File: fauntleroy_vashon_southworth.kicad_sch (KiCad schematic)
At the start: 48 parts

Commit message: pier 50 routing checkpoint
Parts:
- added LED533, LED595: WS2812B-2020, EasyEDA:LED-SMD_4P-L2.0-W2.0-TL_WS2812B-2020, symbol EasyEDA:WS2812B-2020
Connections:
- net +VLED: now also LED533.4 (VDD), LED595.4 (VDD)
- net GND: now also LED533.2 (GND), LED595.2 (GND)
- net at LED581.1 (DO): now also LED595.3 (DI)
- net at LED531.1 (DO): now also LED533.3 (DI)

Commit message: single ferry track checkpoint
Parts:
- removed LED533, LED559, LED560, LED561, LED562, LED563, LED564, LED565, LED566, LED567, LED568, LED569, LED570, LED571, LED572, LED573, LED574, LED576, LED577, LED578, LED579, LED580, LED581, LED595: WS2812B-2020, EasyEDA:LED-SMD_4P-L2.0-W2.0-TL_WS2812B-2020, symbol EasyEDA:WS2812B-2020

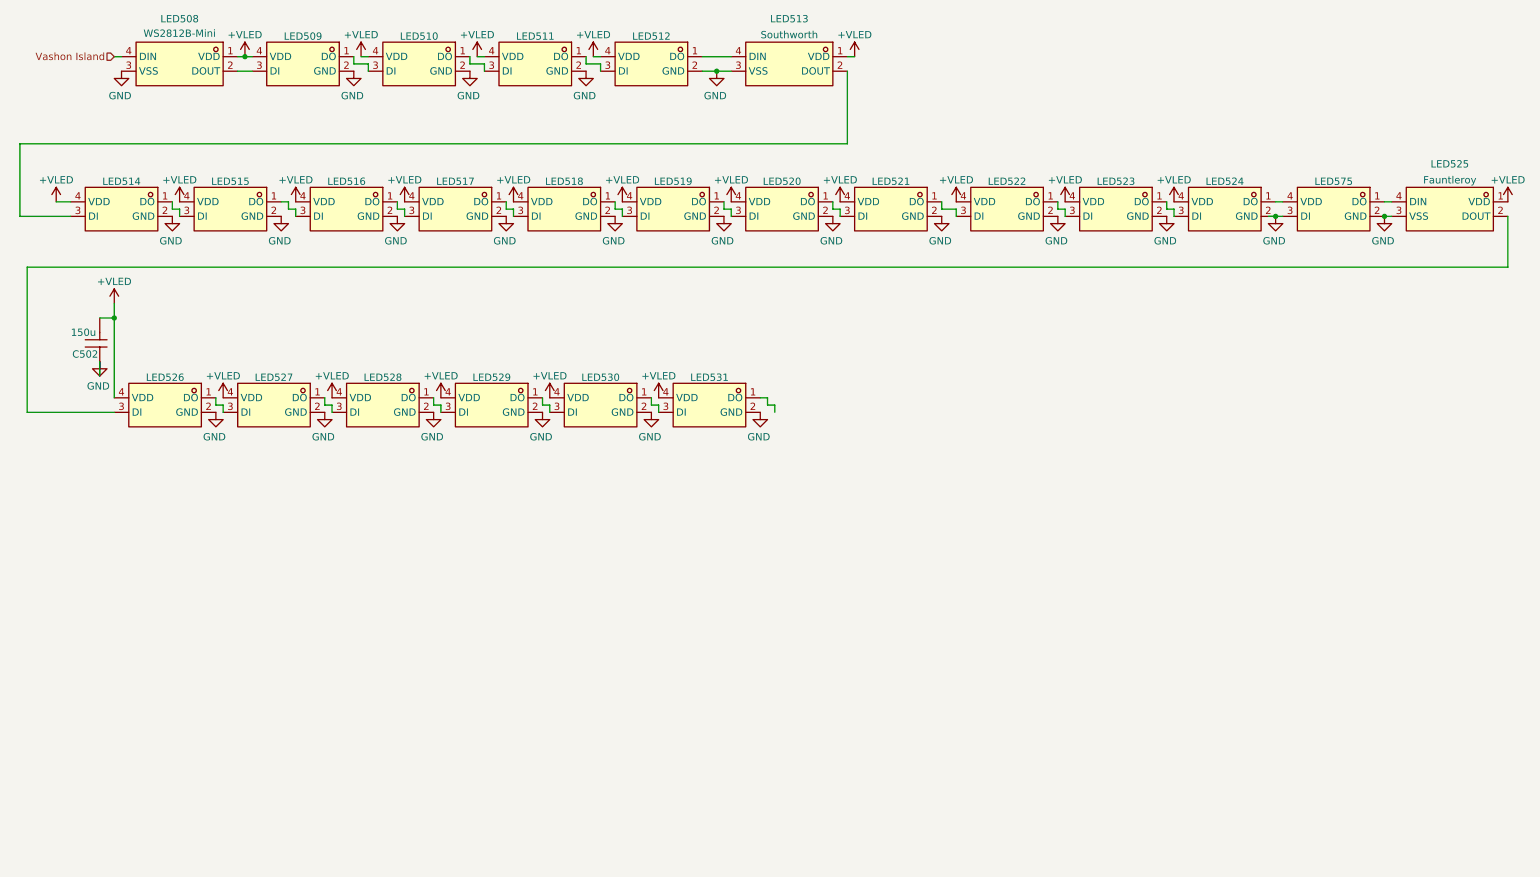
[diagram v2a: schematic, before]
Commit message: Add rail labels
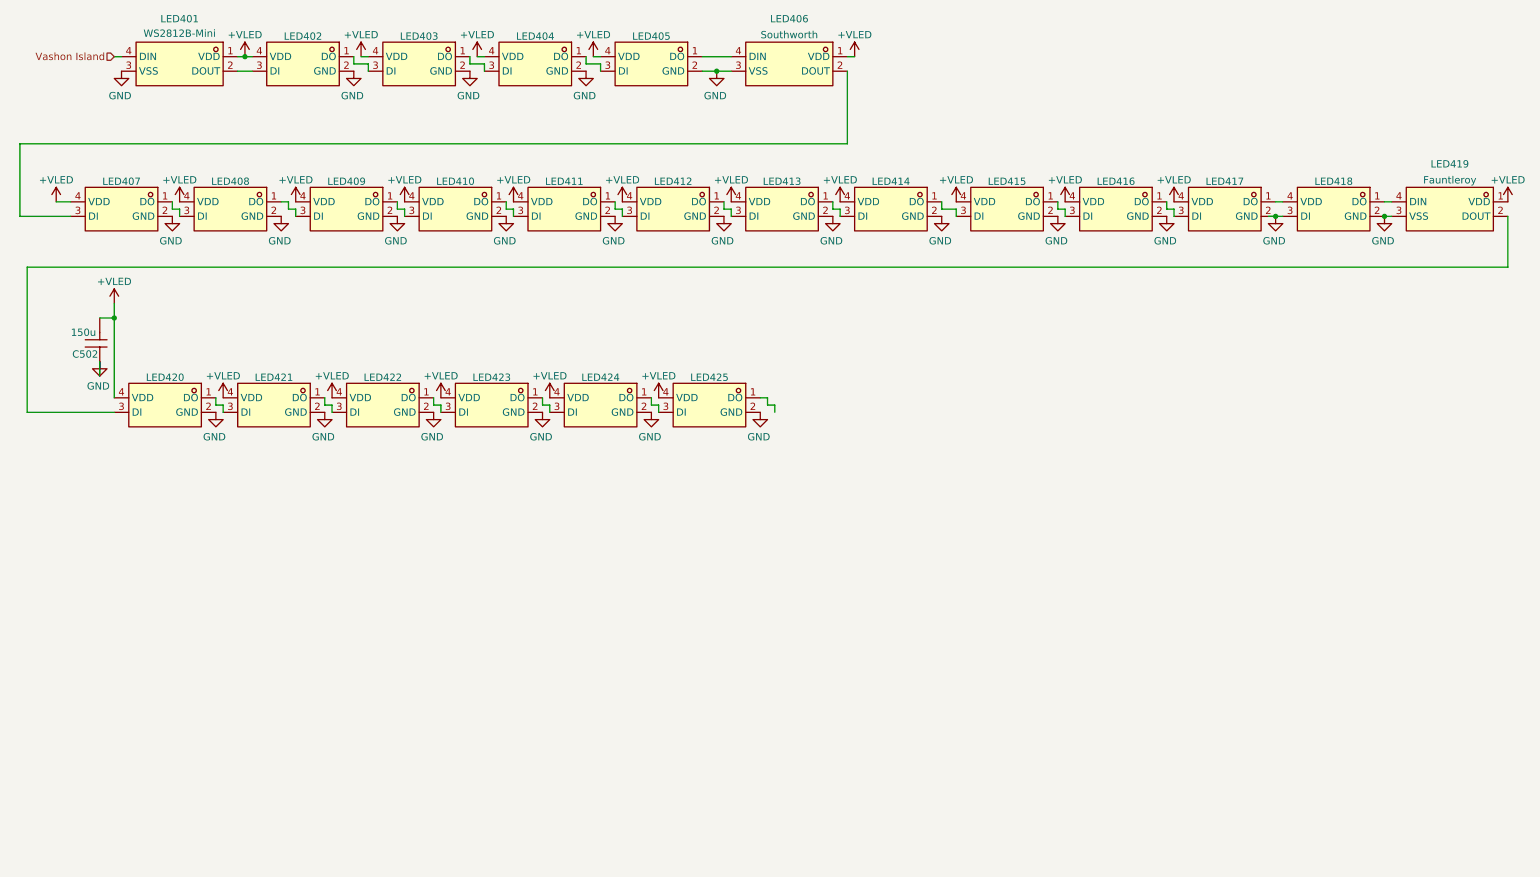
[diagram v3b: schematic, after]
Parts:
- renumbered LED508 to LED401, LED509 to LED402, LED510 to LED403, LED511 to LED404, LED512 to LED405, LED513 to LED406, LED514 to LED407, LED515 to LED408, LED516 to LED409, LED517 to LED410, LED518 to LED411, LED519 to LED412, LED520 to LED413, LED521 to LED414, LED522 to LED415, LED523 to LED416, LED524 to LED417, LED575 to LED418, LED525 to LED419, LED526 to LED420, LED527 to LED421, LED528 to LED422, LED529 to LED423, LED530 to LED424, LED531 to LED425
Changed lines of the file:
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@@
 		(in_pos_files yes)
 		(dnp no)
-		(property "Reference" "LED519"
+		(property "Reference" "LED412"
 			(at 129.54 49.784 0)
 			(show_name no)
@@
 			(project "transit"
 				(path "/3763eade-a8c8-4ec0-9cf2-9db4442b4ee5/153adc6e-a3b0-4527-a19a-87e28aab4b4d/05540940-fa5a-4ea4-af45-fef4388174b4"
-					(reference "LED519")
+					(reference "LED412")
 					(unit 1)
 				)
@@
 		(in_pos_files yes)
 		(dnp no)
-		(property "Reference" "LED525"
+		(property "Reference" "LED419"
 			(at 265.43 46.736 0)
 			(show_name no)
@@
 			(project "transit"
 				(path "/3763eade-a8c8-4ec0-9cf2-9db4442b4ee5/153adc6e-a3b0-4527-a19a-87e28aab4b4d/05540940-fa5a-4ea4-af45-fef4388174b4"
-					(reference "LED525")
+					(reference "LED419")
 					(unit 1)
 				)
@@
 		(in_pos_files yes)
 		(dnp no)
-		(property "Reference" "LED517"
+		(property "Reference" "LED410"
 			(at 91.44 49.784 0)
 			(show_name no)
@@
 			(project "transit"
 				(path "/3763eade-a8c8-4ec0-9cf2-9db4442b4ee5/153adc6e-a3b0-4527-a19a-87e28aab4b4d/05540940-fa5a-4ea4-af45-fef4388174b4"
-					(reference "LED517")
+					(reference "LED410")
 					(unit 1)
 				)
@@
 		(in_pos_files yes)
 		(dnp no)
-		(property "Reference" "LED528"
+		(property "Reference" "LED422"
 			(at 78.74 84.074 0)
 			(show_name no)
@@
 			(project "transit"
 				(path "/3763eade-a8c8-4ec0-9cf2-9db4442b4ee5/153adc6e-a3b0-4527-a19a-87e28aab4b4d/05540940-fa5a-4ea4-af45-fef4388174b4"
-					(reference "LED528")
+					(reference "LED422")
 					(unit 1)
 				)
@@
 		(in_pos_files yes)
 		(dnp no)
-		(property "Reference" "LED526"
+		(property "Reference" "LED420"
 			(at 40.64 84.074 0)
 			(show_name no)
@@
 			(project "transit"
 				(path "/3763eade-a8c8-4ec0-9cf2-9db4442b4ee5/153adc6e-a3b0-4527-a19a-87e28aab4b4d/05540940-fa5a-4ea4-af45-fef4388174b4"
-					(reference "LED526")
+					(reference "LED420")
 					(unit 1)
 				)
@@
 		(in_pos_files yes)
 		(dnp no)
-		(property "Reference" "LED575"
+		(property "Reference" "LED418"
 			(at 245.11 49.784 0)
 			(show_name no)
@@
 			(project "transit"
 				(path "/3763eade-a8c8-4ec0-9cf2-9db4442b4ee5/153adc6e-a3b0-4527-a19a-87e28aab4b4d/05540940-fa5a-4ea4-af45-fef4388174b4"
-					(reference "LED575")
+					(reference "LED418")
 					(unit 1)
 				)
@@
 		(in_pos_files yes)
 		(dnp no)
-		(property "Reference" "LED521"
+		(property "Reference" "LED414"
 			(at 167.64 49.784 0)
 			(show_name no)
@@
 			(project "transit"
 				(path "/3763eade-a8c8-4ec0-9cf2-9db4442b4ee5/153adc6e-a3b0-4527-a19a-87e28aab4b4d/05540940-fa5a-4ea4-af45-fef4388174b4"
-					(reference "LED521")
+					(reference "LED414")
 					(unit 1)
 				)
@@
 		(in_pos_files yes)
 		(dnp no)
-		(property "Reference" "LED524"
+		(property "Reference" "LED417"
 			(at 226.06 49.784 0)
 			(show_name no)
@@
 			(project "transit"
 				(path "/3763eade-a8c8-4ec0-9cf2-9db4442b4ee5/153adc6e-a3b0-4527-a19a-87e28aab4b4d/05540940-fa5a-4ea4-af45-fef4388174b4"
-					(reference "LED524")
+					(reference "LED417")
 					(unit 1)
 				)
@@
 		(in_pos_files yes)
 		(dnp no)
-		(property "Reference" "LED520"
+		(property "Reference" "LED413"
 			(at 148.59 49.784 0)
 			(show_name no)
@@
 			(project "transit"
 				(path "/3763eade-a8c8-4ec0-9cf2-9db4442b4ee5/153adc6e-a3b0-4527-a19a-87e28aab4b4d/05540940-fa5a-4ea4-af45-fef4388174b4"
-					(reference "LED520")
+					(reference "LED413")
 					(unit 1)
 				)
@@
 		(in_pos_files yes)
 		(dnp no)
-		(property "Reference" "LED512"
+		(property "Reference" "LED405"
 			(at 125.73 24.384 0)
 			(show_name no)
@@
 			(project "transit"
 				(path "/3763eade-a8c8-4ec0-9cf2-9db4442b4ee5/153adc6e-a3b0-4527-a19a-87e28aab4b4d/05540940-fa5a-4ea4-af45-fef4388174b4"
-					(reference "LED512")
+					(reference "LED405")
 					(unit 1)
 				)
@@
 		(in_pos_files yes)
 		(dnp no)
-		(property "Reference" "LED515"
+		(property "Reference" "LED408"
 			(at 52.07 49.784 0)
 			(show_name no)
@@
 			(project "transit"
 				(path "/3763eade-a8c8-4ec0-9cf2-9db4442b4ee5/153adc6e-a3b0-4527-a19a-87e28aab4b4d/05540940-fa5a-4ea4-af45-fef4388174b4"
-					(reference "LED515")
+					(reference "LED408")
 					(unit 1)
 				)
@@
 		(in_pos_files yes)
 		(dnp no)
-		(property "Reference" "LED509"
+		(property "Reference" "LED402"
 			(at 64.77 24.384 0)
 			(show_name no)
@@
 			(project "transit"
 				(path "/3763eade-a8c8-4ec0-9cf2-9db4442b4ee5/153adc6e-a3b0-4527-a19a-87e28aab4b4d/05540940-fa5a-4ea4-af45-fef4388174b4"
-					(reference "LED509")
+					(reference "LED402")
 					(unit 1)
 				)
@@
 		(in_pos_files yes)
 		(dnp no)
-		(property "Reference" "LED510"
+		(property "Reference" "LED403"
 			(at 85.09 24.384 0)
 			(show_name no)
@@
 			(project "transit"
 				(path "/3763eade-a8c8-4ec0-9cf2-9db4442b4ee5/153adc6e-a3b0-4527-a19a-87e28aab4b4d/05540940-fa5a-4ea4-af45-fef4388174b4"
-					(reference "LED510")
+					(reference "LED403")
 					(unit 1)
 				)
@@
 		(in_pos_files yes)
 		(dnp no)
-		(property "Reference" "LED514"
+		(property "Reference" "LED407"
 			(at 33.02 49.784 0)
 			(show_name no)
@@
 			(project "transit"
 				(path "/3763eade-a8c8-4ec0-9cf2-9db4442b4ee5/153adc6e-a3b0-4527-a19a-87e28aab4b4d/05540940-fa5a-4ea4-af45-fef4388174b4"
-					(reference "LED514")
+					(reference "LED407")
 					(unit 1)
 				)
@@
 		(in_pos_files yes)
 		(dnp no)
-		(property "Reference" "LED523"
+		(property "Reference" "LED416"
 			(at 207.01 49.784 0)
 			(show_name no)
@@
 			(project "transit"
 				(path "/3763eade-a8c8-4ec0-9cf2-9db4442b4ee5/153adc6e-a3b0-4527-a19a-87e28aab4b4d/05540940-fa5a-4ea4-af45-fef4388174b4"
-					(reference "LED523")
+					(reference "LED416")
 					(unit 1)
 				)
@@
 		(in_pos_files yes)
 		(dnp no)
-		(property "Reference" "LED513"
+		(property "Reference" "LED406"
 			(at 149.86 21.336 0)
 			(show_name no)
@@
 			(project "transit"
 				(path "/3763eade-a8c8-4ec0-9cf2-9db4442b4ee5/153adc6e-a3b0-4527-a19a-87e28aab4b4d/05540940-fa5a-4ea4-af45-fef4388174b4"
-					(reference "LED513")
+					(reference "LED406")
 					(unit 1)
 				)
@@
 		(in_pos_files yes)
 		(dnp no)
-		(property "Reference" "LED527"
+		(property "Reference" "LED421"
 			(at 59.69 84.074 0)
 			(show_name no)
@@
 			(project "transit"
 				(path "/3763eade-a8c8-4ec0-9cf2-9db4442b4ee5/153adc6e-a3b0-4527-a19a-87e28aab4b4d/05540940-fa5a-4ea4-af45-fef4388174b4"
-					(reference "LED527")
+					(reference "LED421")
 					(unit 1)
 				)
@@
 		(in_pos_files yes)
 		(dnp no)
-		(property "Reference" "LED511"
+		(property "Reference" "LED404"
 			(at 105.41 24.384 0)
 			(show_name no)
@@
 			(project "transit"
 				(path "/3763eade-a8c8-4ec0-9cf2-9db4442b4ee5/153adc6e-a3b0-4527-a19a-87e28aab4b4d/05540940-fa5a-4ea4-af45-fef4388174b4"
-					(reference "LED511")
+					(reference "LED404")
 					(unit 1)
 				)
@@
 		(in_pos_files yes)
 		(dnp no)
-		(property "Reference" "LED529"
+		(property "Reference" "LED423"
 			(at 97.79 84.074 0)
 			(show_name no)
@@
 			(project "transit"
 				(path "/3763eade-a8c8-4ec0-9cf2-9db4442b4ee5/153adc6e-a3b0-4527-a19a-87e28aab4b4d/05540940-fa5a-4ea4-af45-fef4388174b4"
-					(reference "LED529")
+					(reference "LED423")
 					(unit 1)
 				)
@@
 		(in_pos_files yes)
 		(dnp no)
-		(property "Reference" "LED518"
+		(property "Reference" "LED411"
 			(at 110.49 49.784 0)
 			(show_name no)
@@
 			(project "transit"
 				(path "/3763eade-a8c8-4ec0-9cf2-9db4442b4ee5/153adc6e-a3b0-4527-a19a-87e28aab4b4d/05540940-fa5a-4ea4-af45-fef4388174b4"
-					(reference "LED518")
+					(reference "LED411")
 					(unit 1)
 				)
@@
 		(in_pos_files yes)
 		(dnp no)
-		(property "Reference" "LED516"
+		(property "Reference" "LED409"
 			(at 72.39 49.784 0)
 			(show_name no)
@@
 			(project "transit"
 				(path "/3763eade-a8c8-4ec0-9cf2-9db4442b4ee5/153adc6e-a3b0-4527-a19a-87e28aab4b4d/05540940-fa5a-4ea4-af45-fef4388174b4"
-					(reference "LED516")
+					(reference "LED409")
 					(unit 1)
 				)
@@
 		(in_pos_files yes)
 		(dnp no)
-		(property "Reference" "LED508"
+		(property "Reference" "LED401"
 			(at 43.18 21.336 0)
 			(show_name no)
@@
 			(project "transit"
 				(path "/3763eade-a8c8-4ec0-9cf2-9db4442b4ee5/153adc6e-a3b0-4527-a19a-87e28aab4b4d/05540940-fa5a-4ea4-af45-fef4388174b4"
-					(reference "LED508")
+					(reference "LED401")
 					(unit 1)
 				)
@@
 		(in_pos_files yes)
 		(dnp no)
-		(property "Reference" "LED530"
+		(property "Reference" "LED424"
 			(at 116.84 84.074 0)
 			(show_name no)
@@
 			(project "transit"
 				(path "/3763eade-a8c8-4ec0-9cf2-9db4442b4ee5/153adc6e-a3b0-4527-a19a-87e28aab4b4d/05540940-fa5a-4ea4-af45-fef4388174b4"
-					(reference "LED530")
+					(reference "LED424")
 					(unit 1)
 				)
@@
 		(in_pos_files yes)
 		(dnp no)
-		(property "Reference" "LED531"
+		(property "Reference" "LED425"
 			(at 135.89 84.074 0)
 			(show_name no)
@@
 			(project "transit"
 				(path "/3763eade-a8c8-4ec0-9cf2-9db4442b4ee5/153adc6e-a3b0-4527-a19a-87e28aab4b4d/05540940-fa5a-4ea4-af45-fef4388174b4"
-					(reference "LED531")
+					(reference "LED425")
 					(unit 1)
 				)
@@
 		(in_pos_files yes)
 		(dnp no)
-		(property "Reference" "LED522"
+		(property "Reference" "LED415"
 			(at 187.96 49.784 0)
 			(show_name no)
@@
 			(project "transit"
 				(path "/3763eade-a8c8-4ec0-9cf2-9db4442b4ee5/153adc6e-a3b0-4527-a19a-87e28aab4b4d/05540940-fa5a-4ea4-af45-fef4388174b4"
-					(reference "LED522")
+					(reference "LED415")
 					(unit 1)
 				)

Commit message: checkpoint
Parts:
- added LED422: WS2812B-2020, EasyEDA:LED-SMD_4P-L2.0-W2.0-TL_WS2812B-2020, symbol EasyEDA:WS2812B-2020
- renumbered LED422 to LED423, LED423 to LED424, LED424 to LED425, LED425 to LED426
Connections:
- net +VLED: now also LED422.4 (VDD)
- net GND: now also LED422.2 (GND)
- net at LED423.3 (DI): now also LED422.1 (DO); no longer LED421.1 (DO)
- new net: LED421.1 (DO), LED422.3 (DI)
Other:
- moved on the sheet: LED423, LED424, LED425, LED426

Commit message: junction checkpoint
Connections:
- net +VLED: now also LED418.4 (VDD)
- net GND: no longer LED418.3 (DI)
- net at LED417.1 (DO): now also LED418.3 (DI); no longer LED418.4 (VDD)
- net FVS_SEATTLE: now reaches LED426.1 (DO)
- net Vashon Island renamed TAHLEQUAH_VASHON
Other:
- moved on the sheet: LED401, LED402, LED403, LED404, LED405, LED406

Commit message: routing complete
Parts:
- removed C502: 150u, EasyEDA:CAP-SMD_L3.5-W2.8, symbol EasyEDA:CL21B106KOQNNNE
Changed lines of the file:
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@@
 	)
 	(junction
-		(at 31.75 73.66)
-		(diameter 0)
-		(color 0 0 0 0)
-	)
-	(junction
 		(at 149.225 31.75)
 		(diameter 0)
@@
 	(wire
 		(pts
-			(xy 29.21 73.66) (xy 31.75 73.66)
-		)
-		(stroke
-			(width 0)
-			(type default)
-		)
-	)
-	(wire
-		(pts
 			(xy 149.225 31.75) (xy 151.765 31.75)
 		)
@@
 	(wire
 		(pts
-			(xy 31.75 71.12) (xy 31.75 73.66)
-		)
-		(stroke
-			(width 0)
-			(type default)
-		)
-	)
-	(wire
-		(pts
 			(xy 106.68 88.9) (xy 107.95 88.9)
 		)
@@
 	(wire
 		(pts
-			(xy 31.75 73.66) (xy 31.75 87.63)
-		)
-		(stroke
-			(width 0)
-			(type default)
-		)
-	)
-	(wire
-		(pts
 			(xy 49.53 88.9) (xy 50.8 88.9)
 		)
@@
 	(wire
 		(pts
-			(xy 29.21 83.82) (xy 29.21 81.28)
-		)
-		(stroke
-			(width 0)
-			(type default)
-		)
-	)
-	(wire
-		(pts
 			(xy 127 88.9) (xy 127 90.17)
 		)
@@
 	)
 	(symbol
-		(lib_name "CL21B106KOQNNNE_4")
-		(lib_id "EasyEDA:CL21B106KOQNNNE")
-		(at 26.67 72.39 90)
-		(mirror x)
-		(unit 1)
-		(body_style 1)
-		(exclude_from_sim no)
-		(in_bom yes)
-		(on_board yes)
-		(in_pos_files yes)
-		(dnp no)
-		(property "Reference" "C502"
-			(at 26.67 80.01 90)
-			(show_name no)
-			(do_not_autoplace no)
-			(effects
-				(font
-					(size 1.27 1.27)
-				)
-			)
-		)
-		(property "Value" "150u"
-			(at 28.575 76.2 90)
-			(show_name no)
-			(do_not_autoplace no)
-			(effects
-				(font
-					(size 1.27 1.27)
-				)
-				(justify left)
-			)
-		)
-		(property "Footprint" "EasyEDA:CAP-SMD_L3.5-W2.8"
-			(at 36.83 72.39 0)
-			(hide yes)
-			(show_name no)
-			(do_not_autoplace no)
-			(effects
-				(font
-					(size 1.27 1.27)
-				)
-			)
-		)
-		(property "Datasheet" "https://www.lcsc.com/datasheet/C212682.pdf"
-			(at 39.37 72.39 0)
-			(hide yes)
-			(show_name no)
-			(do_not_autoplace no)
-			(effects
-				(font
-					(size 1.27 1.27)
-				)
-			)
-		)
-		(property "Description" "150uF ±20% 6.3V Tantalum Capacitors 35mΩ@100kHz CASE-B-3528-21(mm)"
-			(at 26.67 72.39 0)
-			(hide yes)
-			(show_name no)
-			(do_not_autoplace no)
-			(effects
-				(font
-					(size 1.27 1.27)
-				)
-			)
-		)
-		(property "LCSC Part" "C212682"
-			(at 41.91 72.39 0)
-			(hide yes)
-			(show_name no)
-			(do_not_autoplace no)
-			(effects
-				(font
-					(size 1.27 1.27)
-				)
-			)
-		)
-		(pin "2"
-		)
-		(pin "1"
-		)
-		(instances
-			(project "transit"
-				(path "/3763eade-a8c8-4ec0-9cf2-9db4442b4ee5/153adc6e-a3b0-4527-a19a-87e28aab4b4d/05540940-fa5a-4ea4-af45-fef4388174b4"
-					(reference "C502")
-					(unit 1)
-				)
-			)
-		)
-	)
-	(symbol
 		(lib_id "power:GND")
 		(at 144.78 90.17 0)
@@
 	)
 	(symbol
-		(lib_id "power:GND")
-		(at 29.21 81.28 0)
-		(unit 1)
-		(body_style 1)
-		(exclude_from_sim no)
-		(in_bom yes)
-		(on_board yes)
-		(in_pos_files yes)
-		(dnp no)
-		(property "Reference" "#PWR0250"
-			(at 29.21 87.63 0)
-			(hide yes)
-			(show_name no)
-			(do_not_autoplace no)
-			(effects
-				(font
-					(size 1.27 1.27)
-				)
-			)
-		)
-		(property "Value" "GND"
-			(at 28.956 85.598 0)
-			(show_name no)
-			(do_not_autoplace no)
-			(effects
-				(font
-					(size 1.27 1.27)
-				)
-			)
-		)
-		(property "Footprint" ""
-			(at 29.21 81.28 0)
-			(hide yes)
-			(show_name no)
-			(do_not_autoplace no)
-			(effects
-				(font
-					(size 1.27 1.27)
-				)
-			)
-		)
-		(property "Datasheet" ""
-			(at 29.21 81.28 0)
-			(hide yes)
-			(show_name no)
-			(do_not_autoplace no)
-			(effects
-				(font
-					(size 1.27 1.27)
-				)
-			)
-		)
-		(property "Description" "Power symbol creates a global label with name \"GND\" , ground"
-			(at 29.21 81.28 0)
-			(hide yes)
-			(show_name no)
-			(do_not_autoplace no)
-			(effects
-				(font
-					(size 1.27 1.27)
-				)
-			)
-		)
-		(pin "1"
-		)
-		(instances
-			(project "transit"
-				(path "/3763eade-a8c8-4ec0-9cf2-9db4442b4ee5/153adc6e-a3b0-4527-a19a-87e28aab4b4d/05540940-fa5a-4ea4-af45-fef4388174b4"
-					(reference "#PWR0250")
-					(unit 1)
-				)
-			)
-		)
-	)
-	(symbol
 		(lib_id "power:VBUS")
 		(at 66.675 29.21 0)
@@
 	(symbol
 		(lib_id "power:VBUS")
-		(at 31.75 71.12 0)
+		(at 31.75 87.63 0)
 		(unit 1)
 		(body_style 1)
@@
 		(dnp no)
 		(property "Reference" "#PWR062"
-			(at 31.75 74.93 0)
+			(at 31.75 91.44 0)
 			(hide yes)
 			(show_name no)
@@
 		)
 		(property "Value" "+VLED"
-			(at 31.75 67.31 0)
+			(at 31.75 83.82 0)
 			(show_name no)
 			(do_not_autoplace no)
@@
 		)
 		(property "Footprint" ""
-			(at 31.75 71.12 0)
+			(at 31.75 87.63 0)
 			(hide yes)
 			(show_name no)
@@
 		)
 		(property "Datasheet" ""
-			(at 31.75 71.12 0)
+			(at 31.75 87.63 0)
 			(hide yes)
 			(show_name no)
@@
 		)
 		(property "Description" "Power symbol creates a global label with name \"VBUS\""
-			(at 31.75 71.12 0)
+			(at 31.75 87.63 0)
 			(hide yes)
 			(show_name no)
